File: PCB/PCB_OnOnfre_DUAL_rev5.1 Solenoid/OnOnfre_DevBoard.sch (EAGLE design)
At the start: 28 parts, among them J1 9PIN 2.54MM, J3Y S8050, J7 8p, K1 PA1A-6VV, K2 PA1A-6VV, U2 esp12

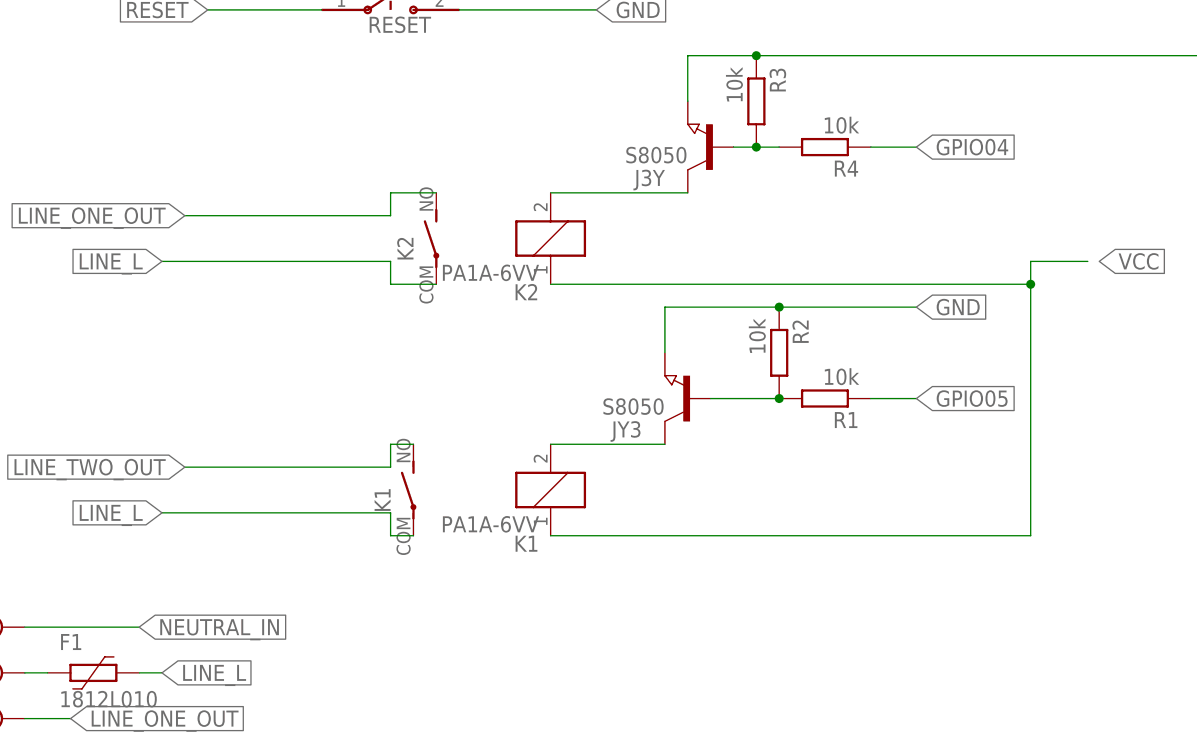
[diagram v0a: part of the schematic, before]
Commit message: Revert "sol"
This reverts commit 5e2c5b42127c6a8382e434407ba92e7f1eb271ca.
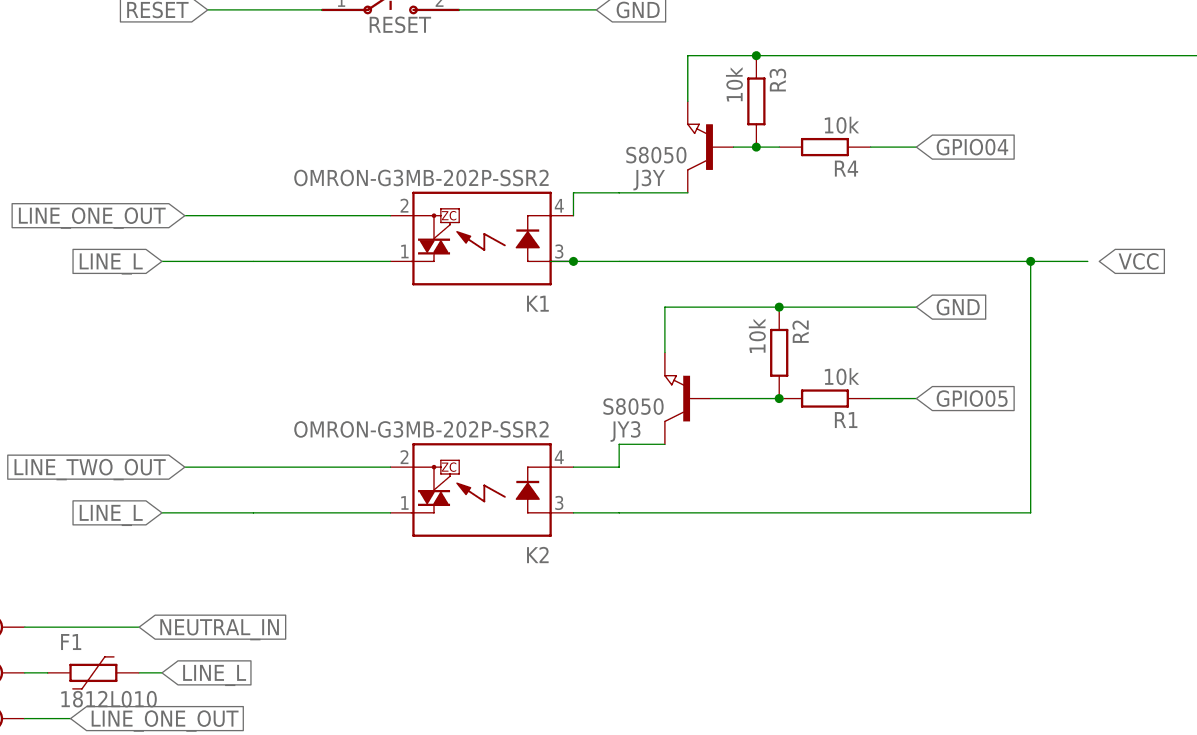
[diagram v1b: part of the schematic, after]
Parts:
- K1, K2: value PA1A-6VV -> OMRON-G3MB-202P-SSR2; device relay:PA1A-6VV -> Omron G3MB 202p SSR:OMRON-G3MB-202P-SSR2
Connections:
- net LINE_L: now also K1.DS1, K2.DS1; no longer K12.P, K22.P
- net LINE_ONE_OUT: now also K1.DS2; no longer K22.S
- net LINE_TWO_OUT: now also K2.DS2; no longer K12.S
- net N$1: now also K1.K; no longer K21.2
- net N$9: now also K2.K; no longer K11.2
- net VCC: now also K1.A, K2.A; no longer K11.1, K21.1
